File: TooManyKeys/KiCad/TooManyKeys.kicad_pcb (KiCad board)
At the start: 2 copper layers, 430.2 x 141.3 mm, 394 parts, among them J1 54104-3031_Oled, J2 AVR-ISP-6, SW1 SW_Push, U1 PRTR5V0U2X, U2 AT90USB1286-AU, U3 PCA9306, U4 AZ1117CH-3.3TRG1, Y1 16MHz

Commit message: After extensive work
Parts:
- removed MX_F10: MX-NoLED, MX_Only:MXOnly-1U-NoLED_3Pins
- moved R14 23.8 mm to (428.2, 254.0), turned to 0 degrees
- moved R13 21.0 mm to (424.7, 252.0)
- moved C14 6.47 mm to (426.7, 258.1)
- moved F1 3.09 mm to (578.1, 256.5)
- moved C26 2.16 mm to (322.1, 253.7)
- moved C27 2.16 mm to (320.0, 253.7)
- moved C13 2.09 mm to (422.7, 266.7)
- moved C16 0.71 mm to (420.6, 252.5)
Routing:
- net GND: track 368.7 -> 101.4 mm, vias 32 -> 83
- net SW10: track 592.4 -> 639.9 mm, vias 33 -> 2
- net SW19: track 440.7 -> 472.2 mm, vias 35 -> 8
- net SW16: track 427.0 -> 457.5 mm, vias 34 -> 2
- net SW7: track 554.1 -> 581.6 mm, vias 37 -> 6
- net CS19: track 295.1 -> 268.6 mm
- net +5V: track 460.7 -> 486.6 mm, vias 8 -> 13
- net CS8: track 256.9 -> 276.6 mm
- net SCL_3.3: track 302.5 -> 318.4 mm
- net SDA_3.3: track 304.8 -> 317.7 mm
- net CS7: track 283.8 -> 271.0 mm
- net COL12: track 266.9 -> 254.2 mm
- net SW1: track 733.9 -> 745.8 mm, vias 32 -> 7
- net SW11: track 489.9 -> 500.7 mm
- net COL14: track 212.6 -> 203.0 mm
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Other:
- net class Power: trace_width 0.381 -> 0.254

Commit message: Updated Logo
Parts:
- removed the G*** at (483.4, 339.7)
- added G***: LOGO, Bitmap:Logo-Alt, B.Cu at (486.0, 340.7)

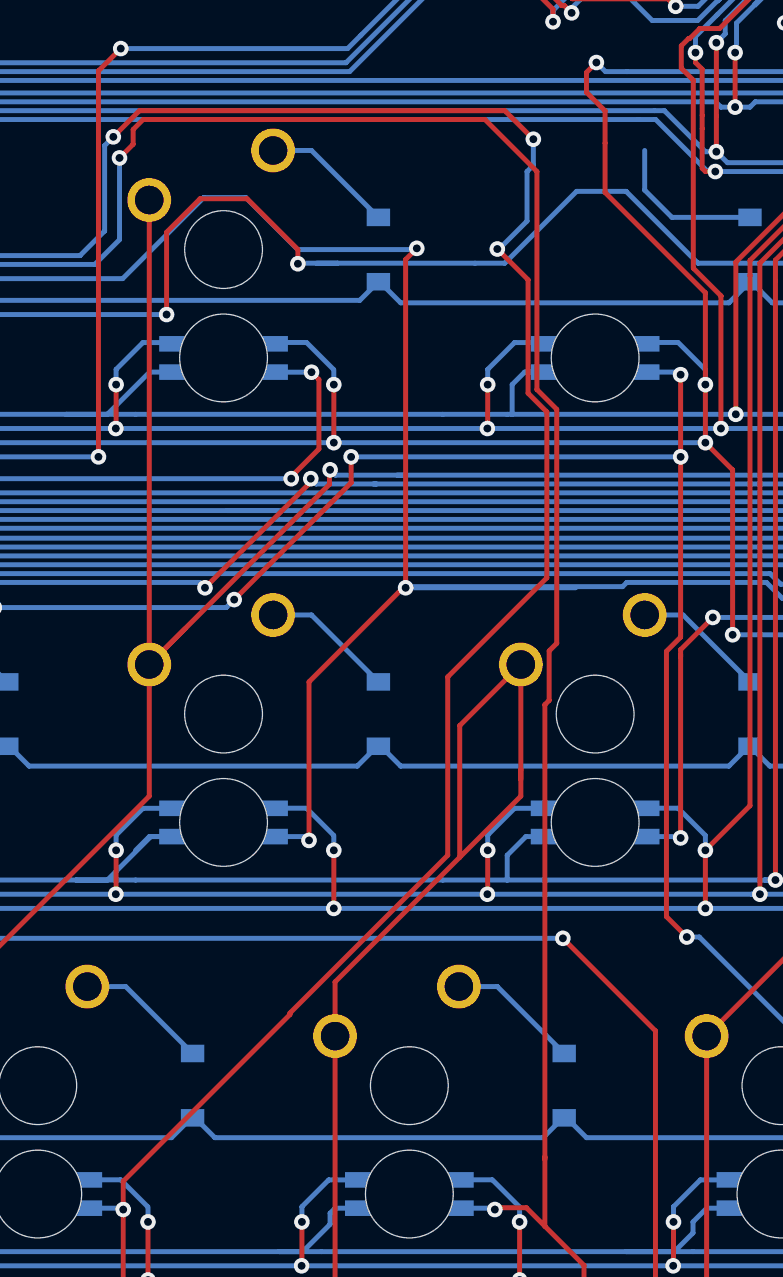
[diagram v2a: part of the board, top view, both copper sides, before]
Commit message: Missing F10 key
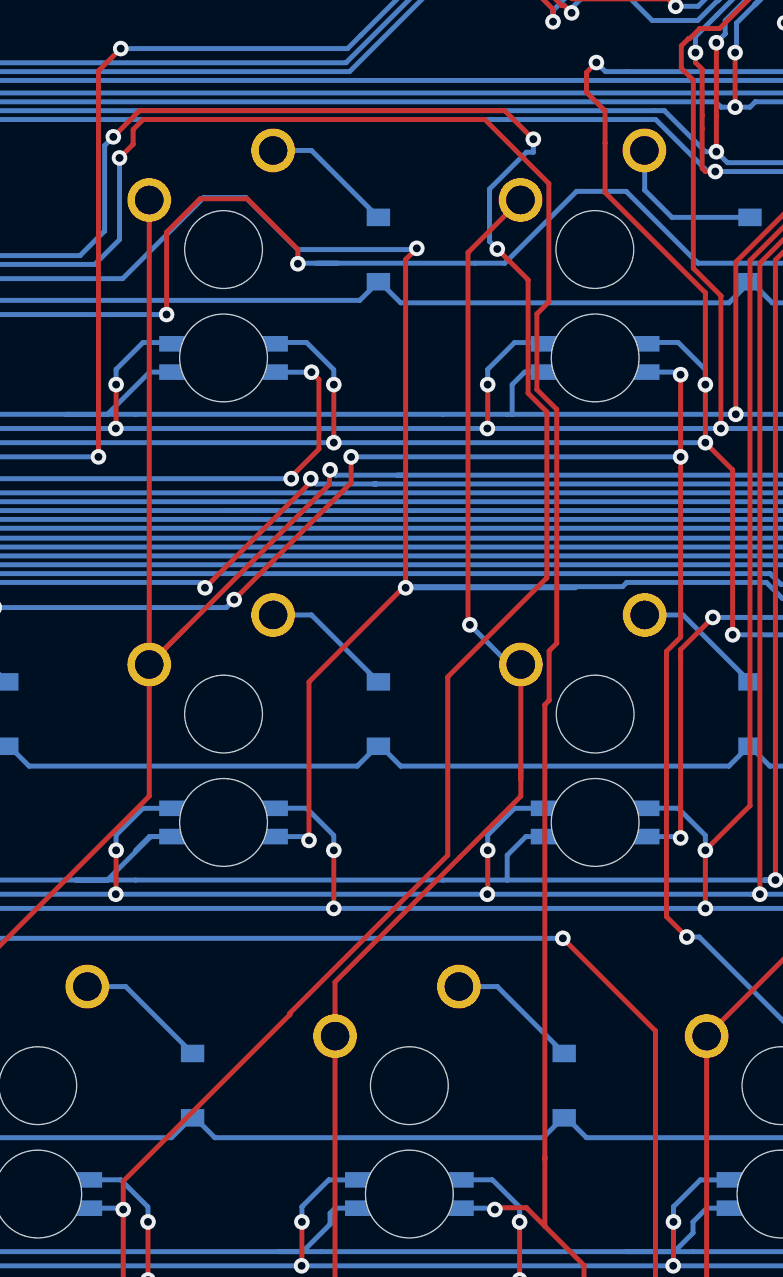
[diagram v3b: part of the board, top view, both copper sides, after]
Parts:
- added MX_F10: MX-NoLED, SamacSys_Parts:MXOnly-1U-NoLED_3Pins, F.Cu at (404.8, 277.8)
- moved G*** 0.15 mm to (486.1, 340.8)
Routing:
- net COL12: track 254.2 -> 269.4 mm, vias 3 -> 4
- net CS12: track 364.4 -> 364.9 mm

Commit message: Final Version of Schematic and PCB
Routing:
- net SW2: track 767.5 -> 795.5 mm
- net SW18: track 479.0 -> 452.4 mm
- net SW3: track 792.3 -> 807.5 mm
- net SW7: track 581.6 -> 576.1 mm
- net SW1: track 745.8 -> 751.0 mm
- net CS6: track 295.5 -> 299.0 mm
- net SCL_3.3: track 318.4 -> 315.8 mm
- net CS27: track 358.9 -> 361.2 mm
- net CS15: track 378.7 -> 381.0 mm
- net CS31: track 278.7 -> 280.4 mm
- net CS25: track 356.0 -> 354.8 mm
- net SW8: track 634.7 -> 635.8 mm
- net CS5: track 293.5 -> 294.6 mm
- net SW5: track 767.7 -> 766.6 mm
- net SW9: track 613.2 -> 614.1 mm
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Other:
- board text added: "TooManyKeys V1.0"

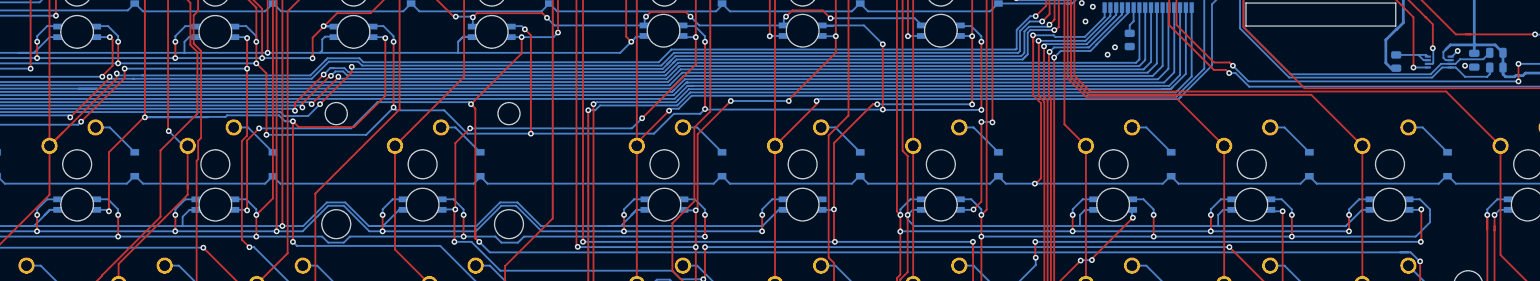
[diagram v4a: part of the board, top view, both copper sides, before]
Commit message: Update for solder mask IC pins of 0.22mm
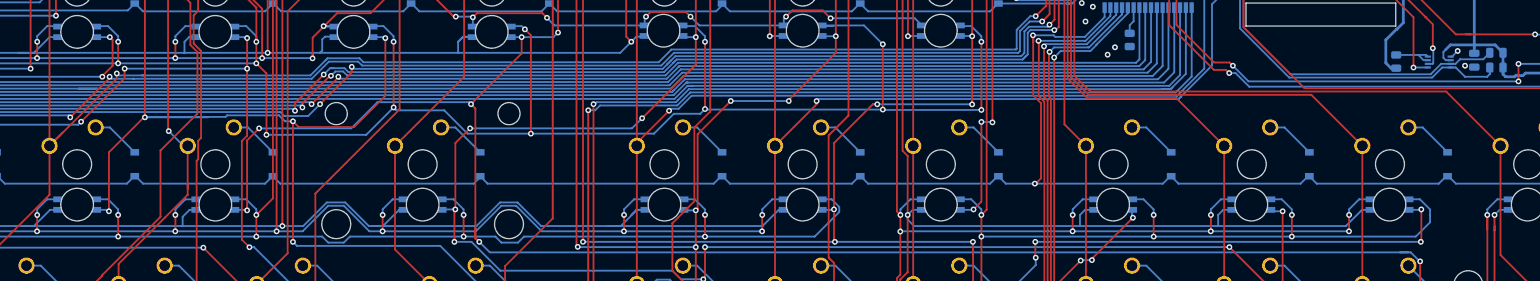
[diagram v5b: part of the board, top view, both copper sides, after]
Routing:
- net SW18: track 452.4 -> 475.8 mm
- net SW16: track 457.5 -> 455.2 mm
- net +5V: track 486.6 -> 487.8 mm
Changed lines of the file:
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@@
     (thickness 1.6)
     (drawings 19)
-    (tracks 6962)
+    (tracks 6968)
     (zones 0)
     (modules 394)
@@
     (pad_drill 0.762)
     (pad_to_mask_clearance 0)
+    (solder_mask_min_width 0.22)
     (aux_axis_origin 0 0)
     (visible_elements 7FFFFFFF)
@@
   (segment (start 578.358 286.324) (end 578.358 274.486) (width 0.381) (layer B.Cu) (net 10) (status 10))
   (segment (start 575.06701 285.16749) (end 574.38925 285.84525) (width 0.381) (layer B.Cu) (net 10))
-  (segment (start 581.22799 285.16749) (end 575.06701 285.16749) (width 0.381) (layer B.Cu) (net 10))
   (segment (start 574.1035 286.131) (end 574.38925 285.84525) (width 0.254) (layer B.Cu) (net 10))
   (segment (start 582.3185 288.29) (end 582.3185 289.2025) (width 0.381) (layer B.Cu) (net 10) (status 10))
@@
   (segment (start 339.78798 254.574) (end 344.23449 250.12749) (width 0.381) (layer B.Cu) (net 10))
   (segment (start 334.264 253.426) (end 334.838 253.426) (width 0.254) (layer B.Cu) (net 10) (status 30))
+  (segment (start 578.358 286.324) (end 578.358 285.23776) (width 0.254) (layer B.Cu) (net 10) (status 10))
+  (segment (start 578.358 285.23776) (end 578.42827 285.16749) (width 0.254) (layer B.Cu) (net 10))
+  (segment (start 578.42827 285.16749) (end 575.06701 285.16749) (width 0.381) (layer B.Cu) (net 10))
+  (segment (start 581.22799 285.16749) (end 578.42827 285.16749) (width 0.381) (layer B.Cu) (net 10))
   (segment (start 543.400358 273.158858) (end 546.149777 273.158858) (width 0.254) (layer B.Cu) (net 11) (status 20))
   (segment (start 542.1295 271.888) (end 543.400358 273.158858) (width 0.254) (layer B.Cu) (net 11))
@@
   (segment (start 229.558 307.906) (end 228.854 308.61) (width 0.254) (layer B.Cu) (net 182))
   (segment (start 230.858 307.906) (end 229.558 307.906) (width 0.254) (layer B.Cu) (net 182) (status 10))
-  (segment (start 383.258 307.906) (end 381.958 307.906) (width 0.254) (layer B.Cu) (net 182) (status 10))
-  (segment (start 381.958 307.906) (end 381.254 308.61) (width 0.254) (layer B.Cu) (net 182))
   (segment (start 464.157 307.906) (end 462.857 307.906) (width 0.254) (layer B.Cu) (net 182) (status 10))
   (segment (start 462.857 307.906) (end 462.153 308.61) (width 0.254) (layer B.Cu) (net 182))
@@
   (segment (start 412.75 278.369868) (end 412.75 306.324) (width 0.254) (layer F.Cu) (net 183))
   (segment (start 419.1 272.019868) (end 412.75 278.369868) (width 0.254) (layer F.Cu) (net 183))
+  (segment (start 487.428961 311.588001) (end 472.313 311.588001) (width 0.254) (layer B.Cu) (net 183))
+  (segment (start 490.820001 308.196961) (end 487.428961 311.588001) (width 0.254) (layer B.Cu) (net 183))
+  (segment (start 489.776962 306.456) (end 490.820001 307.499039) (width 0.254) (layer B.Cu) (net 183))
+  (segment (start 490.820001 307.499039) (end 490.820001 308.196961) (width 0.254) (layer B.Cu) (net 183))
+  (segment (start 488.375 306.456) (end 489.776962 306.456) (width 0.254) (layer B.Cu) (net 183) (status 10))
   (segment (start 246.903997 307.832003) (end 246.903997 308.61) (width 0.254) (layer B.Cu) (net 184))
   (segment (start 248.28 306.456) (end 246.903997 307.832003) (width 0.254) (layer B.Cu) (net 184))
